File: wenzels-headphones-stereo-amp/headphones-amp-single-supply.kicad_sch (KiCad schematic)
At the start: 70 parts, among them J1 9V-15V, J2 9V-15V, J3 Input, J4 Headphones out, Q1 BD139, Q2 BD140, Q3 BD139, Q4 BD140, SW1 POWER ON, U1 NE5532

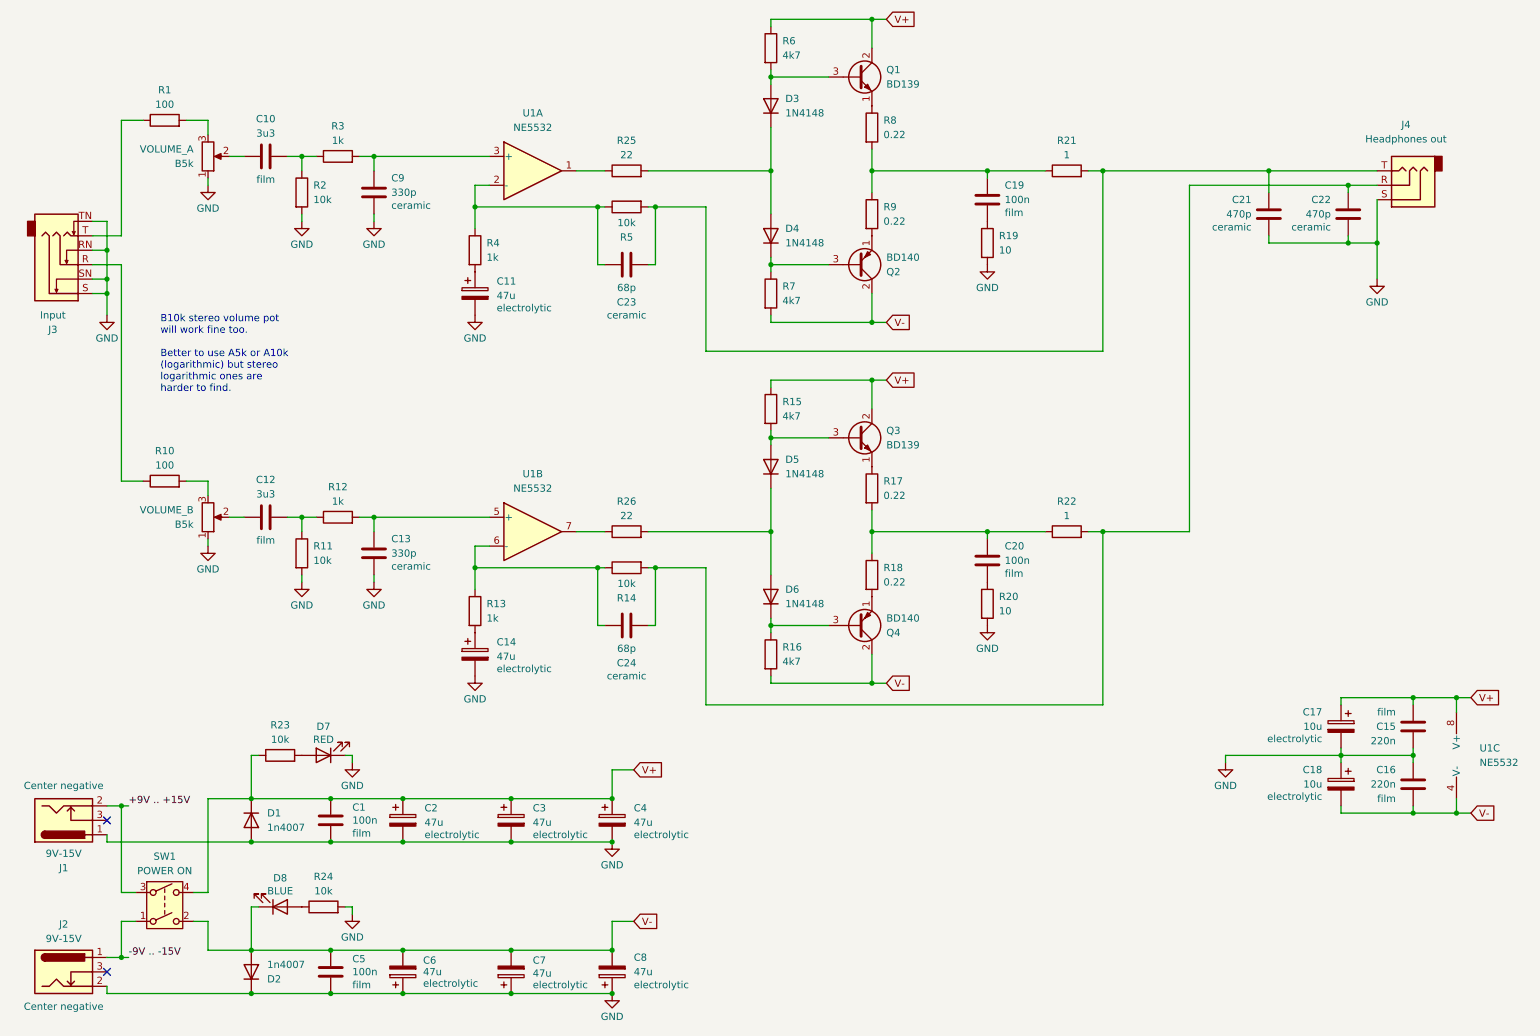
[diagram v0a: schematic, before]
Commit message: wenzels-headphones-stereo-amp: Add single supply schematic variant
- Also make some corrections to both schematics.
- Update next release notes prototype document.
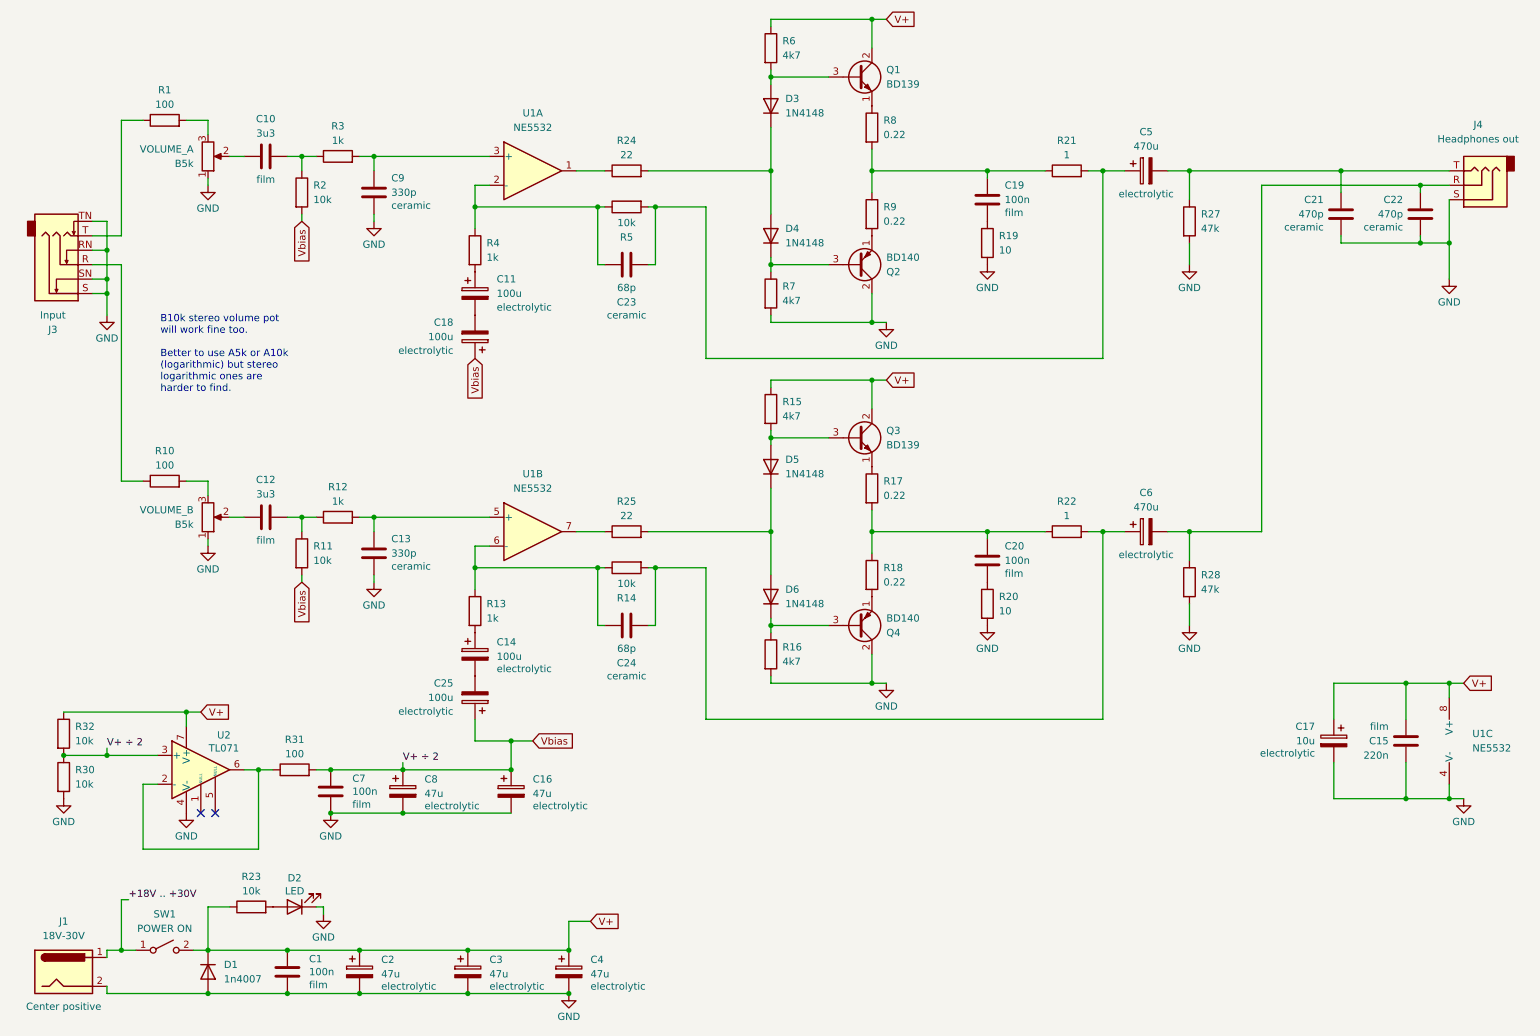
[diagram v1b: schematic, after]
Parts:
- removed C16: 220n, symbol Device:C
- removed C5: 100n, film, symbol Device:C
- removed C7: 47u, electrolytic, symbol Device:C_Polarized
- removed D2: 1n4007, symbol Device:D
- removed D7: RED, symbol Device:LED
- removed D8: BLUE, symbol Device:LED
- removed J1, J2: 9V-15V, symbol Connector:Barrel_Jack_Switch
- removed R26: 22, symbol Device:R
- removed SW1: POWER ON, symbol Switch:SW_DPST
- added C16: 47u, electrolytic, symbol Device:C_Polarized
- added C25: 100u, electrolytic, symbol Device:C_Polarized
- added C5: 470u, symbol Device:C_Polarized
- added C7: 100n, film, symbol Device:C
- added D2: LED, symbol Device:LED
- added J1: 18V-30V, symbol Connector:Jack-DC
- added R27, R28: 47k, symbol Device:R
- added R30, R32: 10k, symbol Device:R
- added R31: 100, symbol Device:R
- added SW1: POWER ON, symbol Switch:SW_SPST
- added U2: TL071, symbol Amplifier_Operational:TL071
- C11, C14: value 47u -> 100u
- C18: value 10u -> 100u
- C6: value 47u -> 470u; footprint electrolytic -> (none); Field5 (none) -> electrolytic
- R24: value 10k -> 22
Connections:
- net GND: now also C8.2, Q2.2 (C), Q4.2 (C), R16.2, R7.2, U1.4 (V-), C16.2, C7.2, D2.1 (K), J1.2, R27.2, R28.2, R30.2, U2.4 (V-); no longer C11.2, C14.2, C18.1, C6.1, C8.1, R11.2, R2.2, R24.2
- net V+: now also R32.1, SW1.2 (B), U2.7 (V+)
- net at R23.2: now also D2.2 (A)
- net at U1.7: now also R25.1
- net at D3.1 (K), D4.2 (A): now also R24.2; no longer R25.2
- net at U1.1: now also R24.1; no longer R25.1
- net at C24.2, R14.2, R22.2: now also C6.1; no longer C22.1, J4.R
- net at C23.2, R21.2, R5.2: now also C5.1; no longer C21.1, J4.T
- net at D5.1 (K), D6.2 (A): now also R25.2
- removed net V-: C18.2, C6.2, C8.2, Q2.2 (C), Q4.2 (C), R16.2, R7.2, U1.4 (V-)
- new net: C22.1, C6.2, J4.R, R28.1
- new net: C14.2, C25.2
- new net: C21.1, C5.2, J4.T, R27.1
- new net: C11.2, C18.2
- new net: R31.1, U2.2 (-), U2.6
- new net +18V .. +30V: J1.1, SW1.1 (A)
- new net Vbias: C16.1, C18.1, C25.1, C7.1, C8.1, R11.2, R2.2, R30.1, R31.2, R32.2, U2.3 (+)
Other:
- title: Wenzel’s Headphones Stereo Amp (dual supply) -> Wenzel’s Headphones Stereo Amp (single supply)
- moved on the sheet: C1, C15, C17, C2, C21, C22, C3, C4, D1, J4, R23, R25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

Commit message: wenzels-headphones-stereo-amp: Mark output caps as >=470u
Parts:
- C5, C6: value 470u -> >=470u
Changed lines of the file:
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@@
 			)
 		)
-		(property "Value" "470u"
+		(property "Value" ">=470u"
 			(at 214.63 104.902 90)
 			(effects
@@
 			)
 		)
-		(property "Value" "470u"
+		(property "Value" ">=470u"
 			(at 214.63 41.402 90)
 			(effects

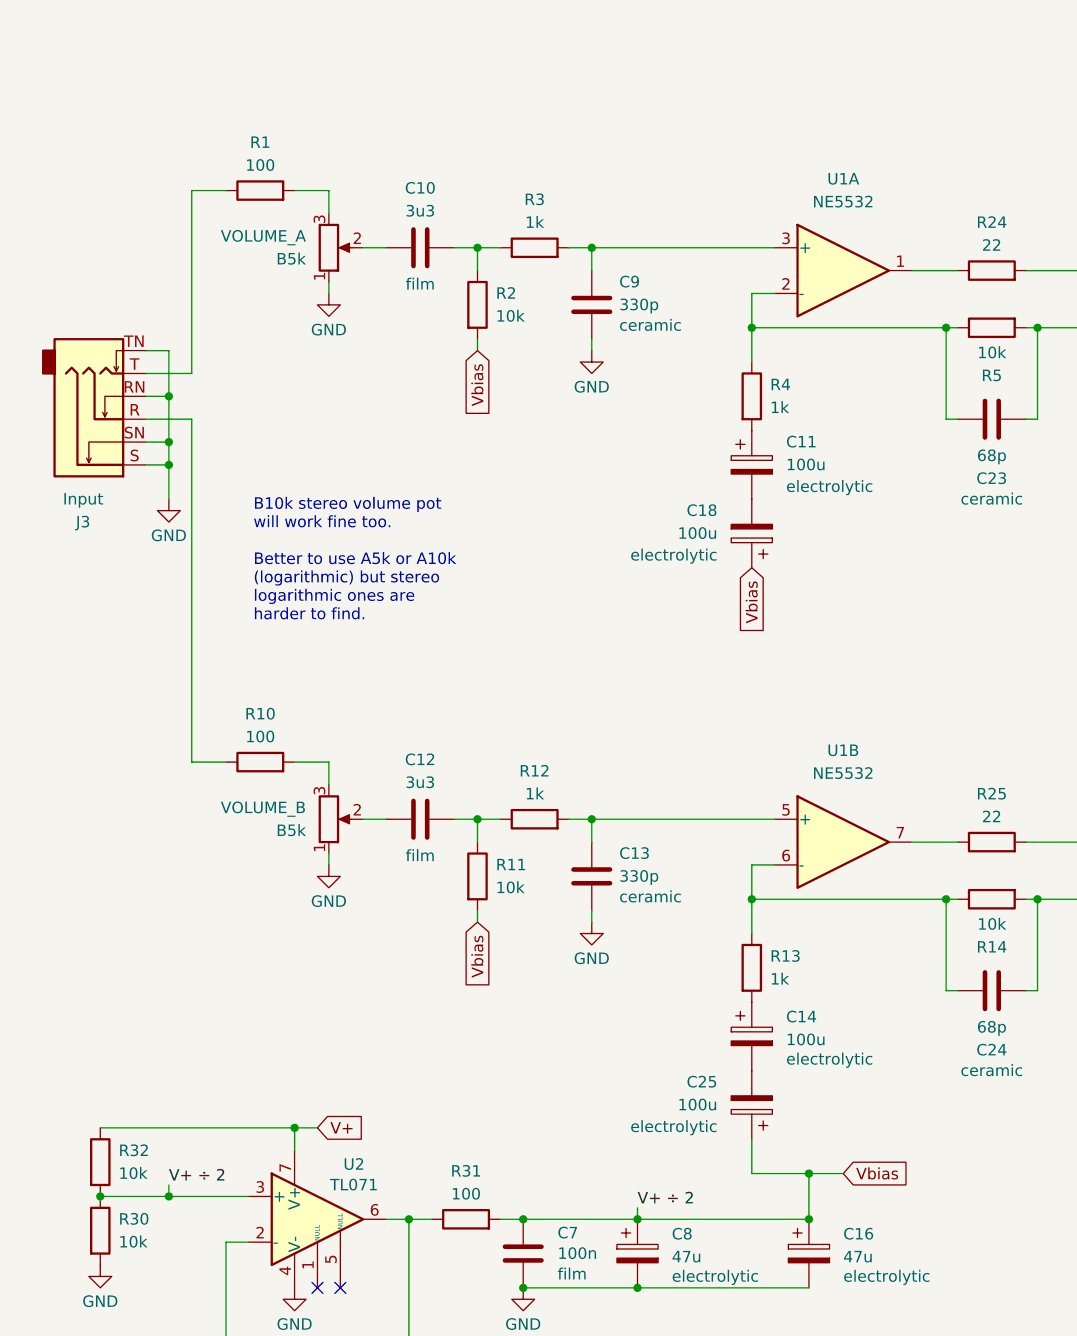
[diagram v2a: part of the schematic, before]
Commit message: wenzels-headphones-stereo-amp: Add GAIN knob
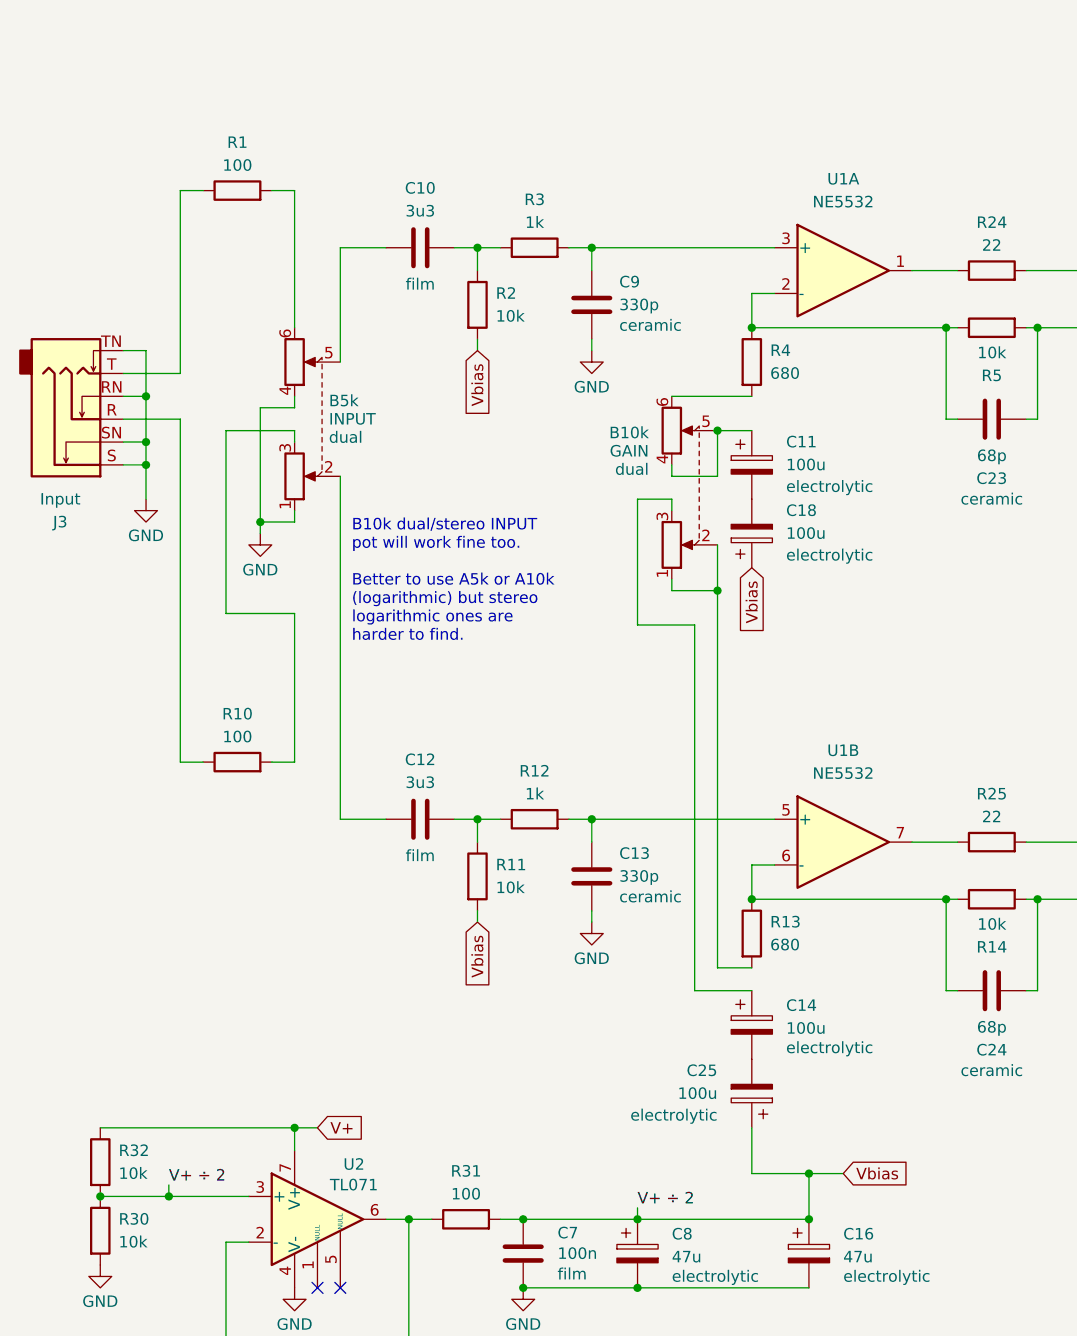
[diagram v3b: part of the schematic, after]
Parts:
- removed VOLUME_A, VOLUME_B: B5k, symbol Device:R_Potentiometer
- added GAIN: B10k, symbol Device:R_Potentiometer_Dual
- added INPUT: B5k, symbol Device:R_Potentiometer_Dual
- R13, R4: value 1k -> 680
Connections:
- net GND: now also INPUT.1, INPUT.4
- net at R4.2: now also GAIN.6; no longer C11.1
- net at C12.1: now also INPUT.2
- net at R1.2: now also INPUT.6
- net at R10.2: now also INPUT.3
- net at C10.1: now also INPUT.5
- net at R13.2: now also GAIN.1, GAIN.2; no longer C14.1
- new net: C11.1, GAIN.4, GAIN.5
- new net: C14.1, GAIN.3
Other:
- note added: "B10k dual/stereo INPUT pot will work fine too. Better to use A5k or A10k (logarithmic) but stereo logarithmic ones are harder to find."
- note removed: "B10k stereo volume pot will work fine too. Better to use A5k or A10k (logarithmic) but stereo logarithmic ones are harder to find."
- moved on the sheet: C14, C18, C25, J3, R1, R10, R13, R4
